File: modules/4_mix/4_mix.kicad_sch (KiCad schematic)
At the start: 11 parts, among them U1 LM358

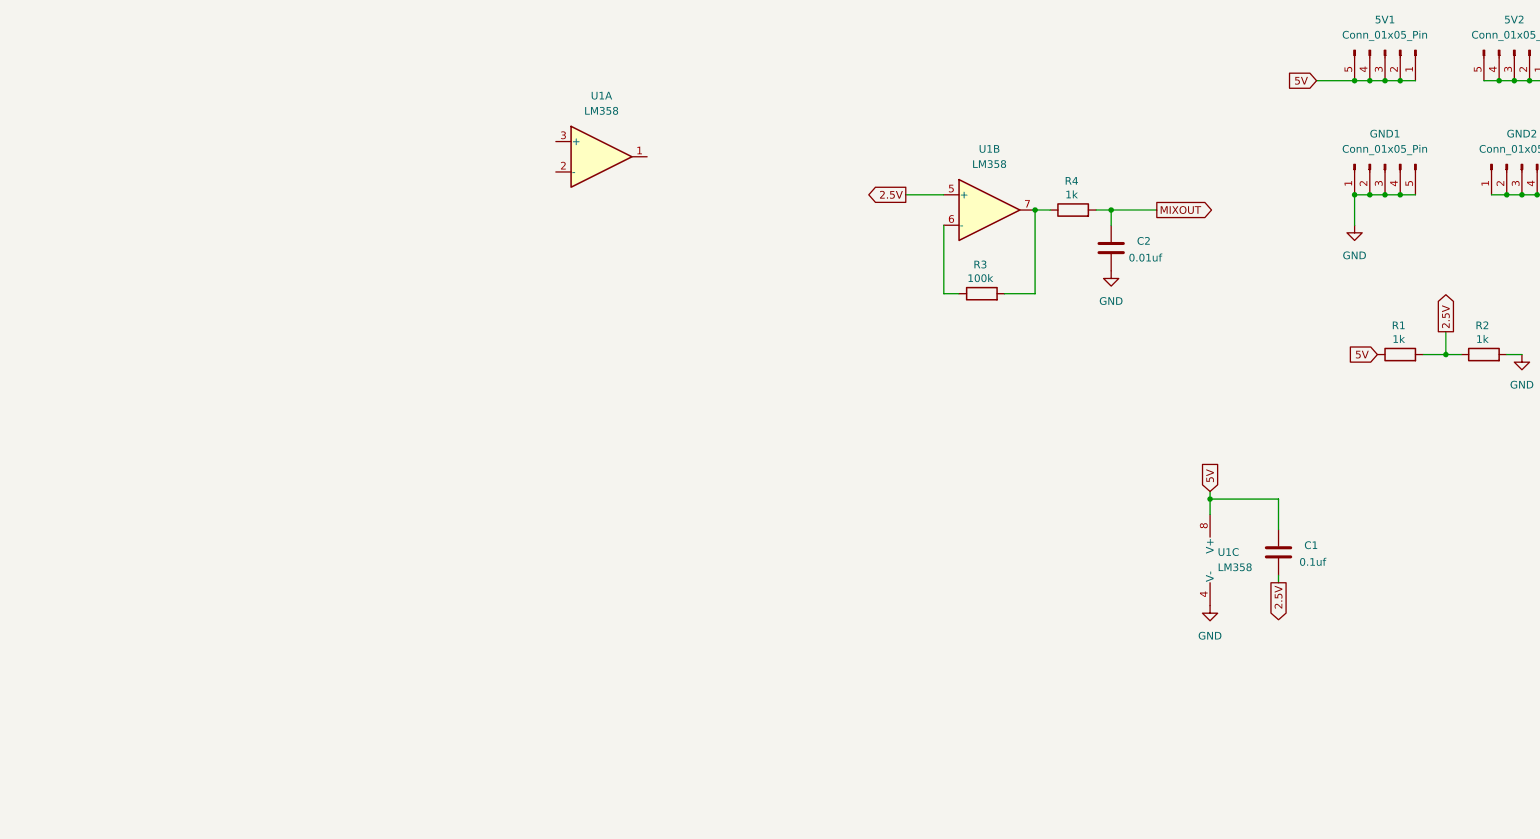
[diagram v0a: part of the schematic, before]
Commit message: Implement the simulation model.
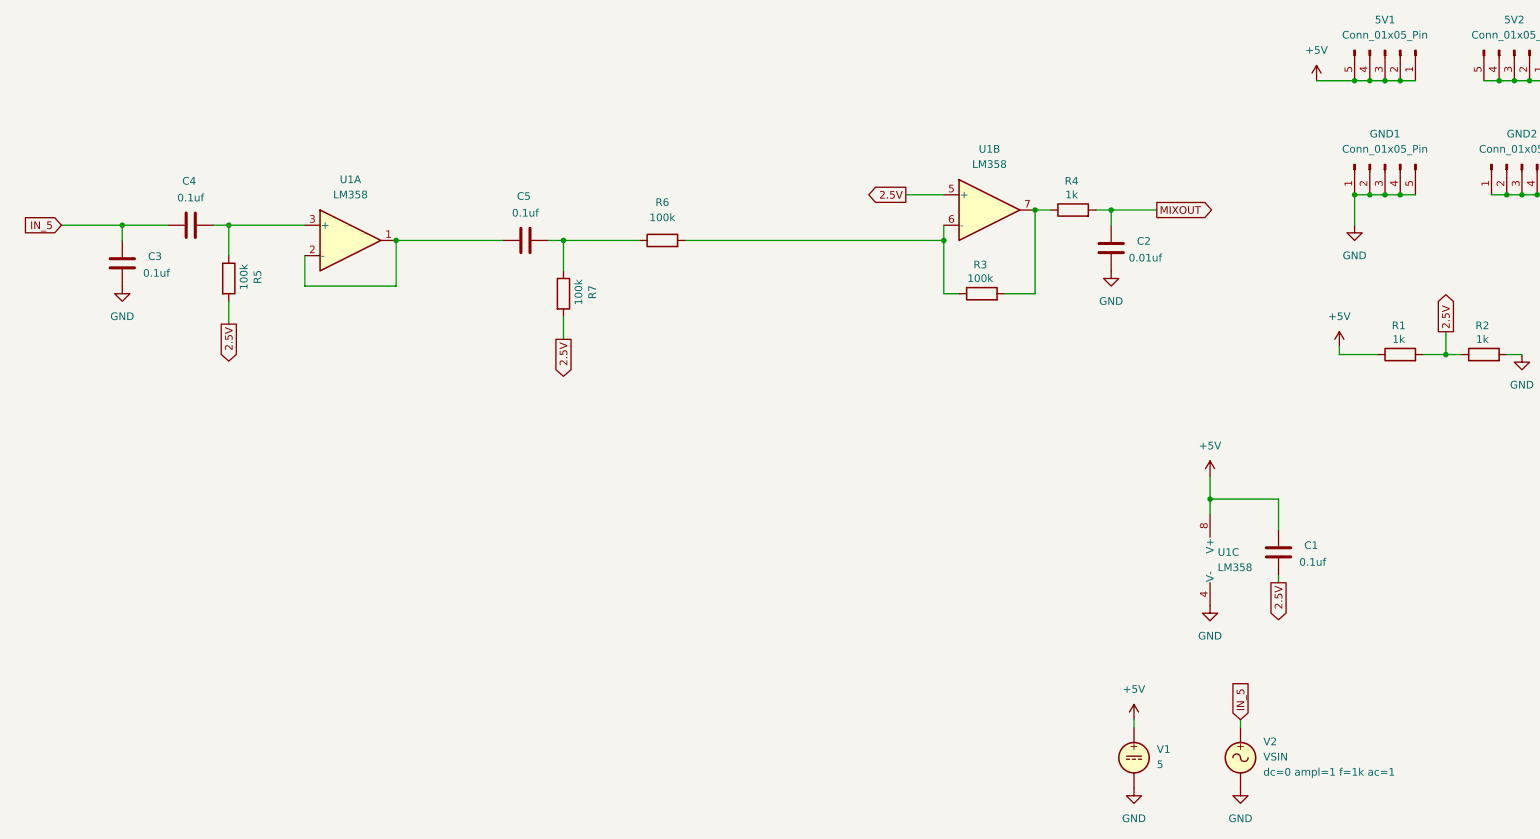
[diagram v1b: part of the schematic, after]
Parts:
- added C3, C4, C5: 0.1uf, symbol Device:C
- added R5, R6, R7: 100k, symbol Device:R
- added V1: 5, symbol Simulation_SPICE:VDC
- added V2: VSIN, symbol Simulation_SPICE:VSIN
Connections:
- net 2.5V: now also R5.2, R7.2
- net GND: now also C3.2, V1.2, V2.2
- net at R3.1, U1.6 (-): now also R6.2
- net at U1.1: now also U1.2 (-), C5.1
- net at U1.3 (+): now also C4.2, R5.1
- net 5V renamed +5V
- net +5V: now also V1.1
- new net: C5.2, R6.1, R7.1
- new net IN_5: C3.1, C4.1, V2.1
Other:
- moved on the sheet: U1A

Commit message: Updated the core design
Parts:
- removed C3, C5: 0.1uf, symbol Device:C
- removed R7: 100k, symbol Device:R
- added RV1: 50k, symbol Device:R_Potentiometer
- C1, C2, C4: footprint (none) -> Capacitor_SMD:C_0402_1005Metric
- R1, R2, R3, R4, R5, R6: footprint (none) -> Resistor_SMD:R_0402_1005Metric
- U1: footprint (none) -> Package_SO:SOIC-8-1EP_3.9x4.9mm_P1.27mm_EP2.29x3mm
- V1, V2: now not fitted
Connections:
- net GND: now also RV1.1
- net at R6.1: now also U1.1, U1.2 (-)
- net IN_5: no longer names the net of C4.1
- net IN_5: now also RV1.2; no longer V2.1
- new net IN_1: RV1.3, V2.1
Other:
- moved on the sheet: C4, R5, R6, U1A

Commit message: Add the full mixer
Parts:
- added C3, C5, C6, C7, C8, C9: 0.1uf, Capacitor_SMD:C_0402_1005Metric, symbol Device:C
- added R10, R11, R12, R13, R14, R7, R8, R9: 100k, Resistor_SMD:R_0402_1005Metric, symbol Device:R
- added R15: 1k, Resistor_SMD:R_0402_1005Metric, symbol Device:R
- added R16: 51k, Resistor_SMD:R_0402_1005Metric, symbol Device:R
- added RV2, RV3, RV4: 50k, symbol Device:R_Potentiometer
- added U2, U3: LM358, Package_SO:SOIC-8-1EP_3.9x4.9mm_P1.27mm_EP2.29x3mm, symbol Amplifier_Operational:LM358
- added V3: VSIN, symbol Simulation_SPICE:VSIN
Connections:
- net +5V: now also C3.1, C7.1, U2.8 (V+), U3.8 (V+)
- net 2.5V: now also C3.2, C7.2, R11.2, R13.2, R7.2, R9.2
- net GND: now also R16.2, RV2.1, RV3.1, RV4.1, U2.4 (V-), U3.4 (V-), V3.2
- net at C4.2, R5.1: now also U2.3 (+); no longer U1.3 (+)
- net at R3.1, R6.2, U1.6 (-): now also R10.2, R12.2, R14.2, R8.2
- net OUT_5: now reaches U1.1, U1.2 (-)
- net OUT_5: now also R14.1; no longer R6.1
- new net: R10.1, U3.1, U3.2 (-)
- new net: C6.2, R9.1, U3.3 (+)
- new net: C9.2, R13.1, U1.3 (+)
- new net: C8.1, RV4.2
- new net: C8.2, R11.1, U3.5 (+)
- new net: C6.1, RV3.2
- new net: R8.1, U2.6 (-), U2.7
- new net: R12.1, U3.6 (-), U3.7
- new net: C9.1, R15.2, R16.1
- new net: C5.1, RV2.2
- new net: R6.1, U2.1, U2.2 (-)
- new net: C5.2, R7.1, U2.5 (+)
- new net IN_2: RV2.3
- new net IN_3: RV3.3
- new net IN_4: RV4.3
- new net IN_5: R15.1, V3.1
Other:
- moved on the sheet: 5V1, 5V2, C1, GND1, GND2, R1, R2, U1C, V1, V2

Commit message: Schematics is done. Now it's time for PCB layout.
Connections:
- net IN_2: now also V3.1
- net IN_5: no longer V3.1
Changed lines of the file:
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@@
 		)
 	)
-	(global_label "IN_5"
+	(global_label "IN_2"
 		(shape input)
 		(at 354.33 139.7 90)

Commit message: Implemented the PCB design of 4_mix
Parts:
- added INPUT1, OUTPUT1: Conn_01x05_Socket, Connector_PinSocket_2.54mm:PinSocket_1x05_P2.54mm_Vertical, symbol Connector:Conn_01x05_Socket
- RV1, RV2, RV3, RV4: footprint (none) -> BreadModular_OPT1:Potentiometer_RV09
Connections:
- net +5V: now also 5V2.1 (Pin_1), 5V2.2 (Pin_2), 5V2.3 (Pin_3), 5V2.4 (Pin_4), 5V2.5 (Pin_5)
- net IN_1: now also INPUT1.1 (Pin_1), OUTPUT1.1 (Pin_1)
- net IN_2: now also INPUT1.2 (Pin_2), OUTPUT1.2 (Pin_2)
- net IN_3: now also INPUT1.3 (Pin_3), OUTPUT1.3 (Pin_3)
- net IN_4: now also INPUT1.4 (Pin_4), OUTPUT1.4 (Pin_4)
- net IN_5: now also INPUT1.5 (Pin_5)
- net MIXOUT: now also OUTPUT1.5 (Pin_5)

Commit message: Use TL072 the current version has some pops and cracks LM358 could be the issue. So, we are trying TL072
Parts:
- RV1, RV2, RV3, RV4: footprint BreadModular_OPT1:Potentiometer_RV09 -> BreadModular_Pots:Potentiometer_RV09
- U1, U2, U3: value LM358 -> TL072
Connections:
- net +5V: no longer C1.1, C3.1, C7.1
- net GND: now also C1.1, C3.1, C7.1
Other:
- moved on the sheet: C1, U1C, U2C, U3C

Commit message: Use MCP6002 in the 4_mix. This provides more headroom due to it's rail-2-rail output.
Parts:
- U1, U2, U3: value TL072 -> MCP6002
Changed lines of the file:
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@@
 			)
 		)
-		(property "Value" "TL072"
+		(property "Value" "MCP6002"
 			(at 91.44 90.17 0)
 			(effects
@@
 			)
 		)
-		(property "Value" "TL072"
+		(property "Value" "MCP6002"
 			(at 330.2 97.7899 0)
 			(effects
@@
 			)
 		)
-		(property "Value" "TL072"
+		(property "Value" "MCP6002"
 			(at 91.44 129.54 0)
 			(effects
@@
 			)
 		)
-		(property "Value" "TL072"
+		(property "Value" "MCP6002"
 			(at 91.44 166.37 0)
 			(effects
@@
 			)
 		)
-		(property "Value" "TL072"
+		(property "Value" "MCP6002"
 			(at 180.34 46.99 0)
 			(effects
@@
 			)
 		)
-		(property "Value" "TL072"
+		(property "Value" "MCP6002"
 			(at 91.44 19.05 0)
 			(effects
@@
 			)
 		)
-		(property "Value" "TL072"
+		(property "Value" "MCP6002"
 			(at 356.87 101.5999 0)
 			(effects
@@
 			)
 		)
-		(property "Value" "TL072"
+		(property "Value" "MCP6002"
 			(at 384.81 101.5999 0)
 			(effects
@@
 			)
 		)
-		(property "Value" "TL072"
+		(property "Value" "MCP6002"
 			(at 91.44 57.15 0)
 			(effects

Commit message: Add missing production files for 4_mix
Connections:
- net IN_1: no longer V2.1
- net IN_2: now also V2.1; no longer V3.1
- net IN_4: now also V3.1
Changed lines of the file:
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@@
 		)
 	)
-	(global_label "IN_1"
+	(global_label "IN_2"
 		(shape input)
 		(at 334.01 139.7 90)
@@
 		)
 	)
-	(global_label "IN_2"
+	(global_label "IN_4"
 		(shape input)
 		(at 354.33 139.7 90)
@@
 			)
 		)
-		(property "Sim.Params" "pos=0.8"
+		(property "Sim.Params" "pos=1.0"
 			(at 36.83 110.236 90)
 			(effects
@@
 			)
 		)
-		(property "Sim.Params" "pos=0.5"
+		(property "Sim.Params" "pos=0.0"
 			(at 36.83 77.216 90)
 			(effects
@@
 			)
 		)
-		(property "Sim.Params" "pos=0.8"
+		(property "Sim.Params" "pos=0.0"
 			(at 36.83 39.116 90)
 			(effects
@@
 			)
 		)
-		(property "Sim.Params" "pos=0.8"
+		(property "Sim.Params" "pos=0"
 			(at 36.83 149.606 90)
 			(effects
